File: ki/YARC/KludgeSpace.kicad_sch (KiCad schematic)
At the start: 3 parts, among them J8 6-PIN FROM MCR, U100 74LS32, U101 74LS157

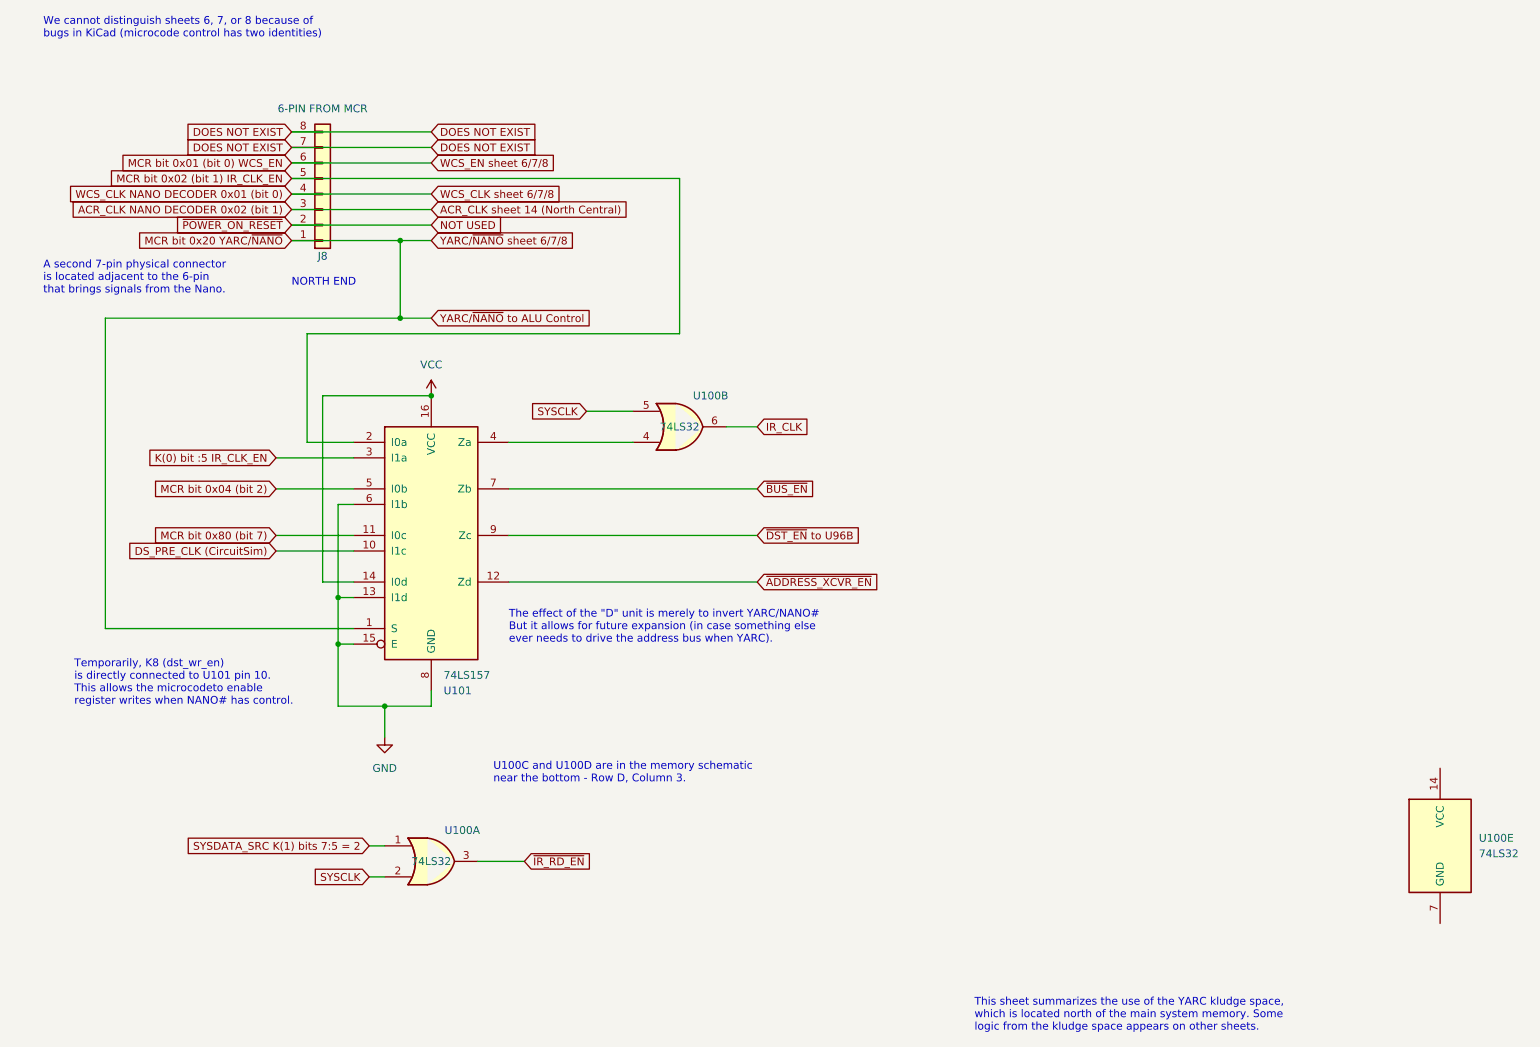
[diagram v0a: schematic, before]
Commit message: Large commit. Document two hardware changes to microcode controls. Adapt Nano firmware to these changes. Significantly simplify initialization logic and make it more consistent about reset.
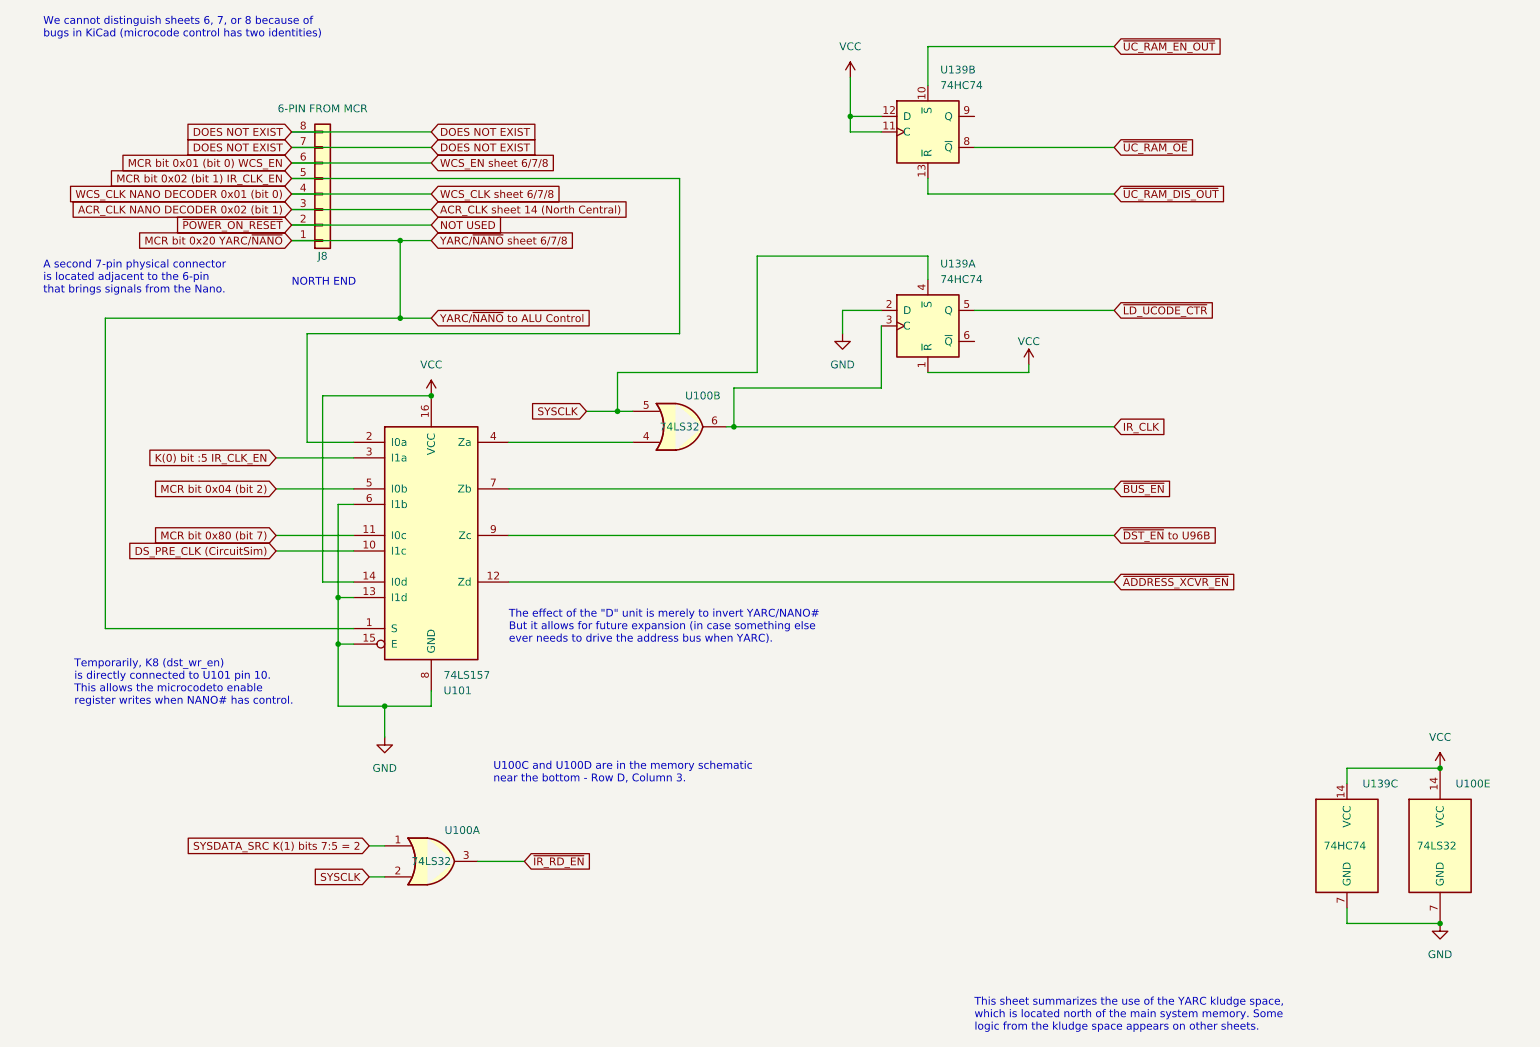
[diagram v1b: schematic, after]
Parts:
- added U139: 74HC74, symbol 74xx:74HC74
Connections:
- net GND: now also U100.7 (GND), U139.2 (D), U139.7 (GND)
- net IR_CLK: now also U139.3 (C)
- net SYSCLK: now also U139.4 (~{S})
- net VCC: now also U100.14 (VCC), U139.1 (~{R}), U139.11 (C), U139.12 (D), U139.14 (VCC)
- new net ~{LD_UCODE_CTR}: U139.5 (Q)
- new net ~{UC_RAM_DIS_OUT}: U139.13 (~{R})
- new net ~{UC_RAM_EN_OUT}: U139.10 (~{S})
- new net ~{UC_RAM_OE}: U139.8 (~{Q})

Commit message: Add delay line for general register write signal. Minor corrections and cleanups.
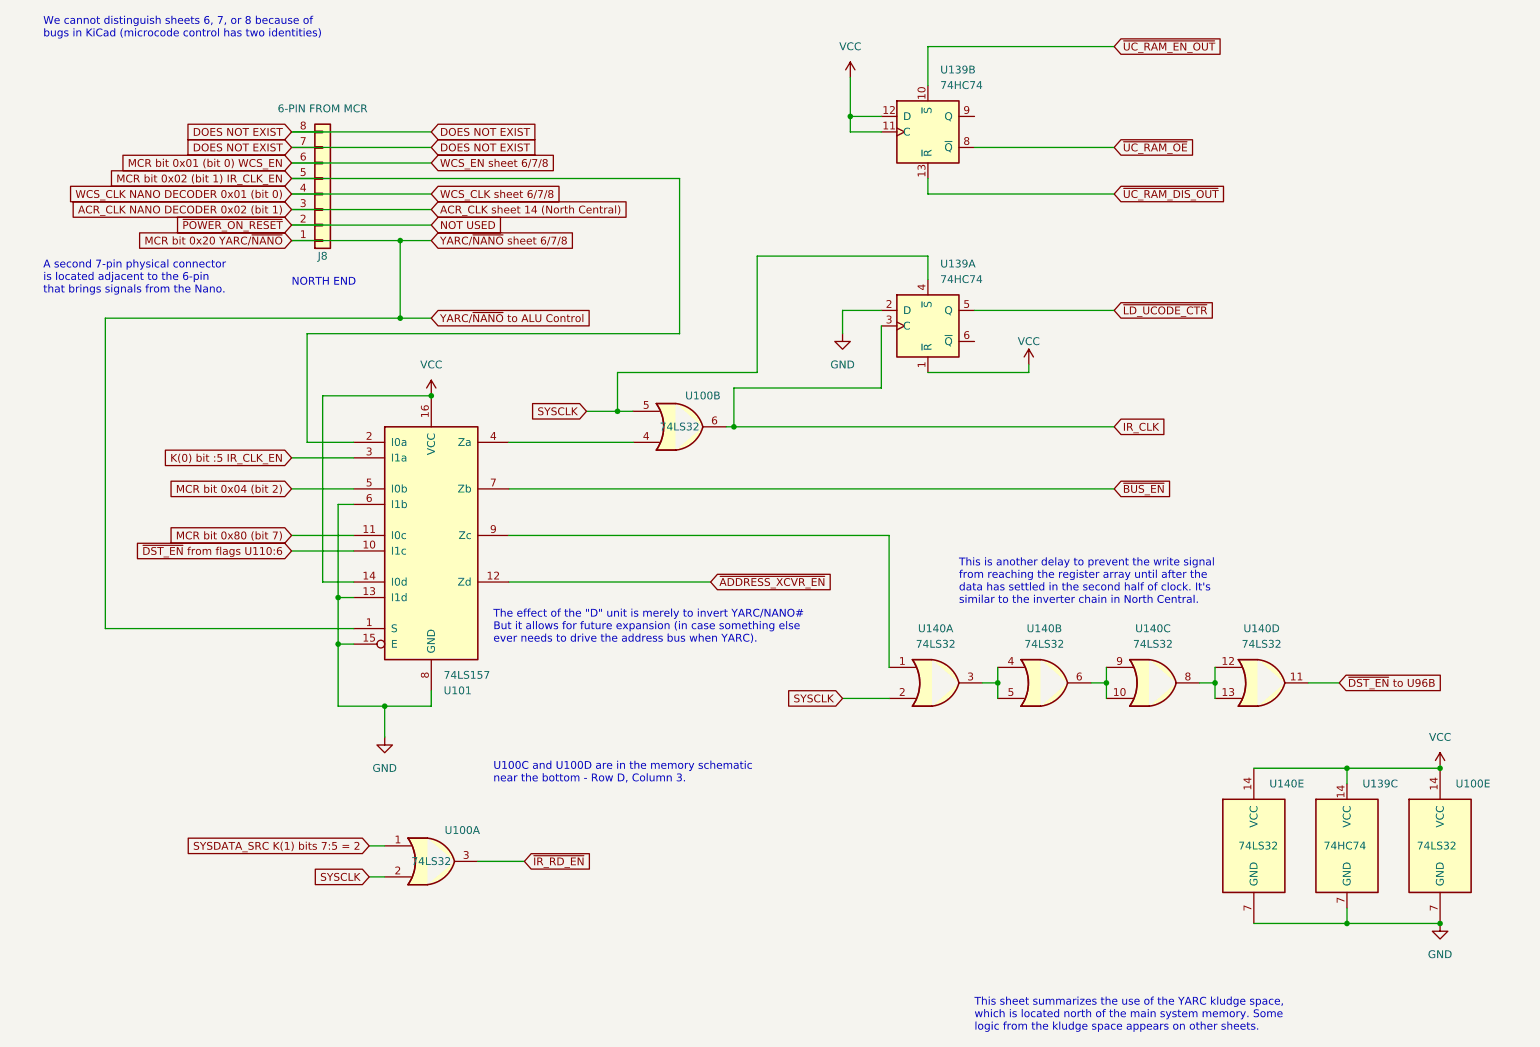
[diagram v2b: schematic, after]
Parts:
- added U140: 74LS32, symbol 74xx:74LS32
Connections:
- net GND: now also U140.7 (GND)
- net SYSCLK: now also U140.2
- net VCC: now also U140.14 (VCC)
- net ~{DST_EN} to U96B: now also U140.11; no longer U101.9 (Zc)
- net DS_PRE_CLK (CircuitSim) renamed ~{DST_EN} from flags U110:6
- new net: U101.9 (Zc), U140.1
- new net: U140.3, U140.4, U140.5
- new net: U140.10, U140.6, U140.9
- new net: U140.12, U140.13, U140.8
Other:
- note added: "This is another delay to prevent the write signal from reaching the register array until after the data has settled in the second half of clock. It's similar to the inverter chain in North Central."
- note removed: "Temporarily, K8 (dst_wr_en) is directly connected to U101 pin 10. This allows the microcodeto enable register writes when NANO# has control."
